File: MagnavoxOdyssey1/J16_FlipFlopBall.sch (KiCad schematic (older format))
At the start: 15 parts

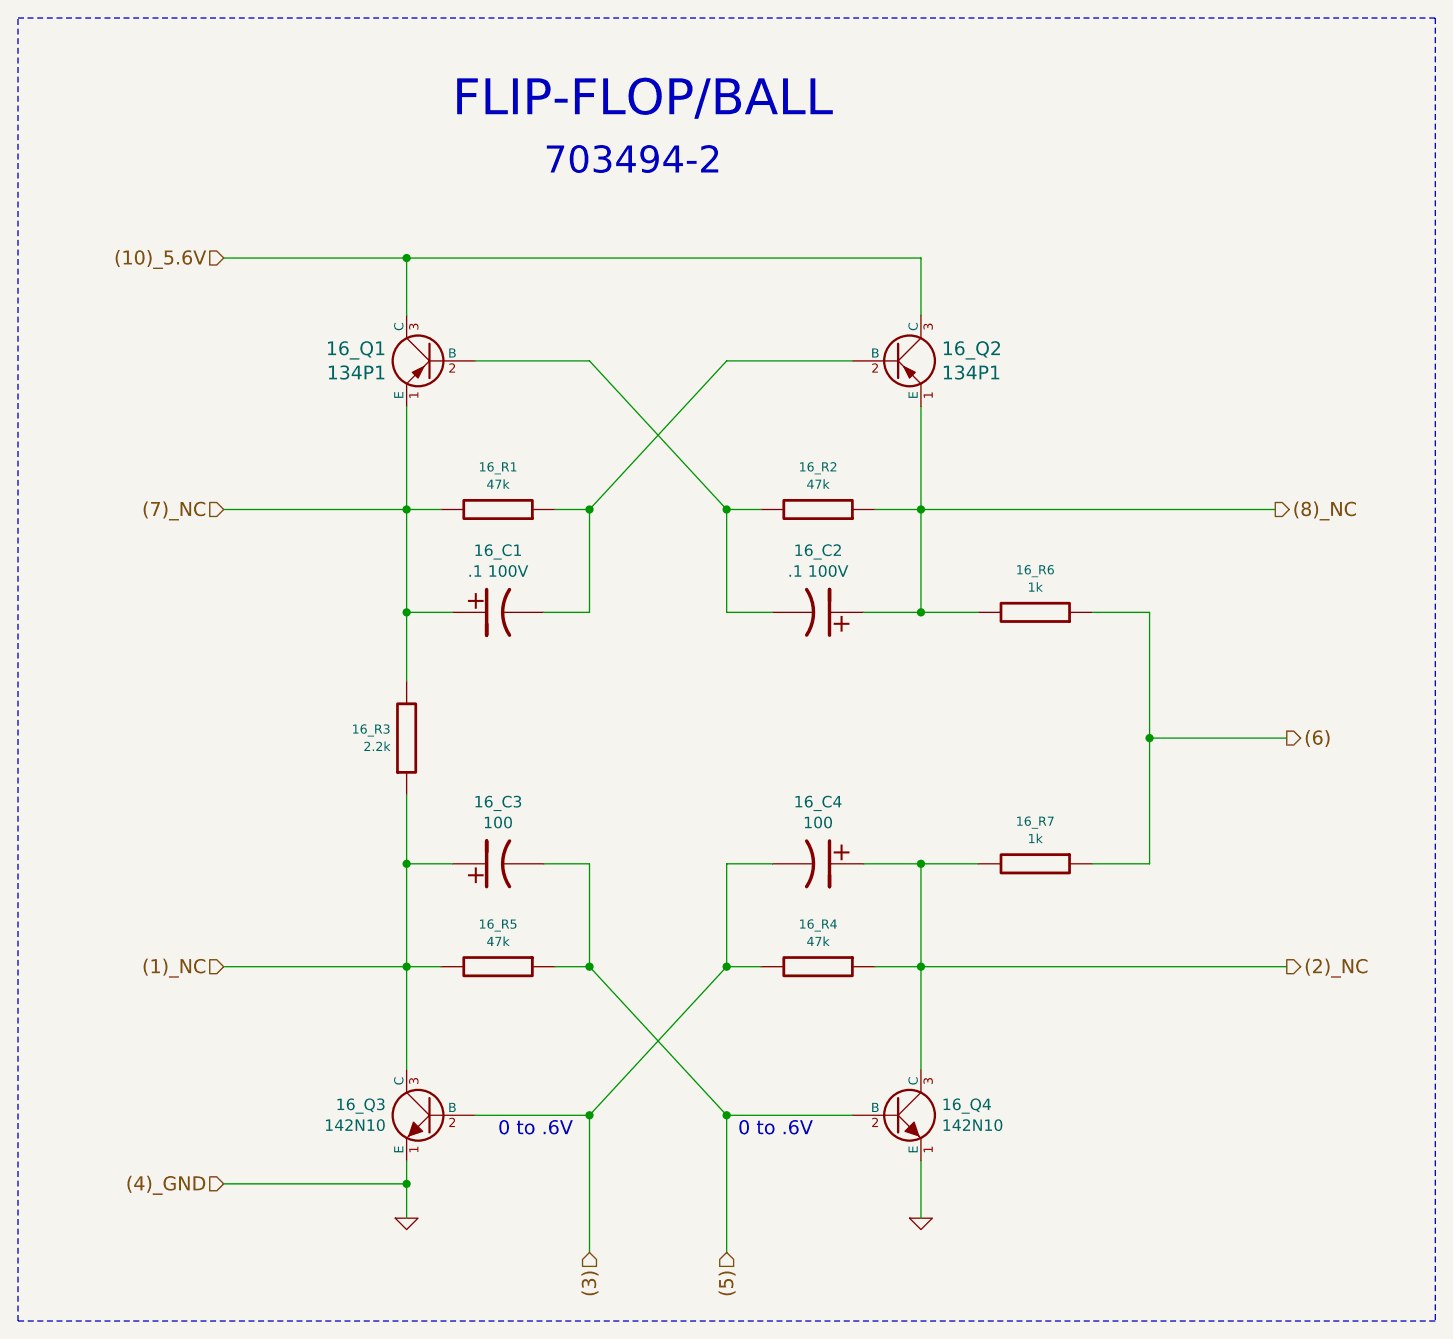
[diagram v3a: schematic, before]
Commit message: terminei de transcrever a PCB toda. Deixei de fora de propósito o estágio de modulação RF do sinal. É pouca coisa, posso adicionar amanhã ou depois... Gerei também um PDFão
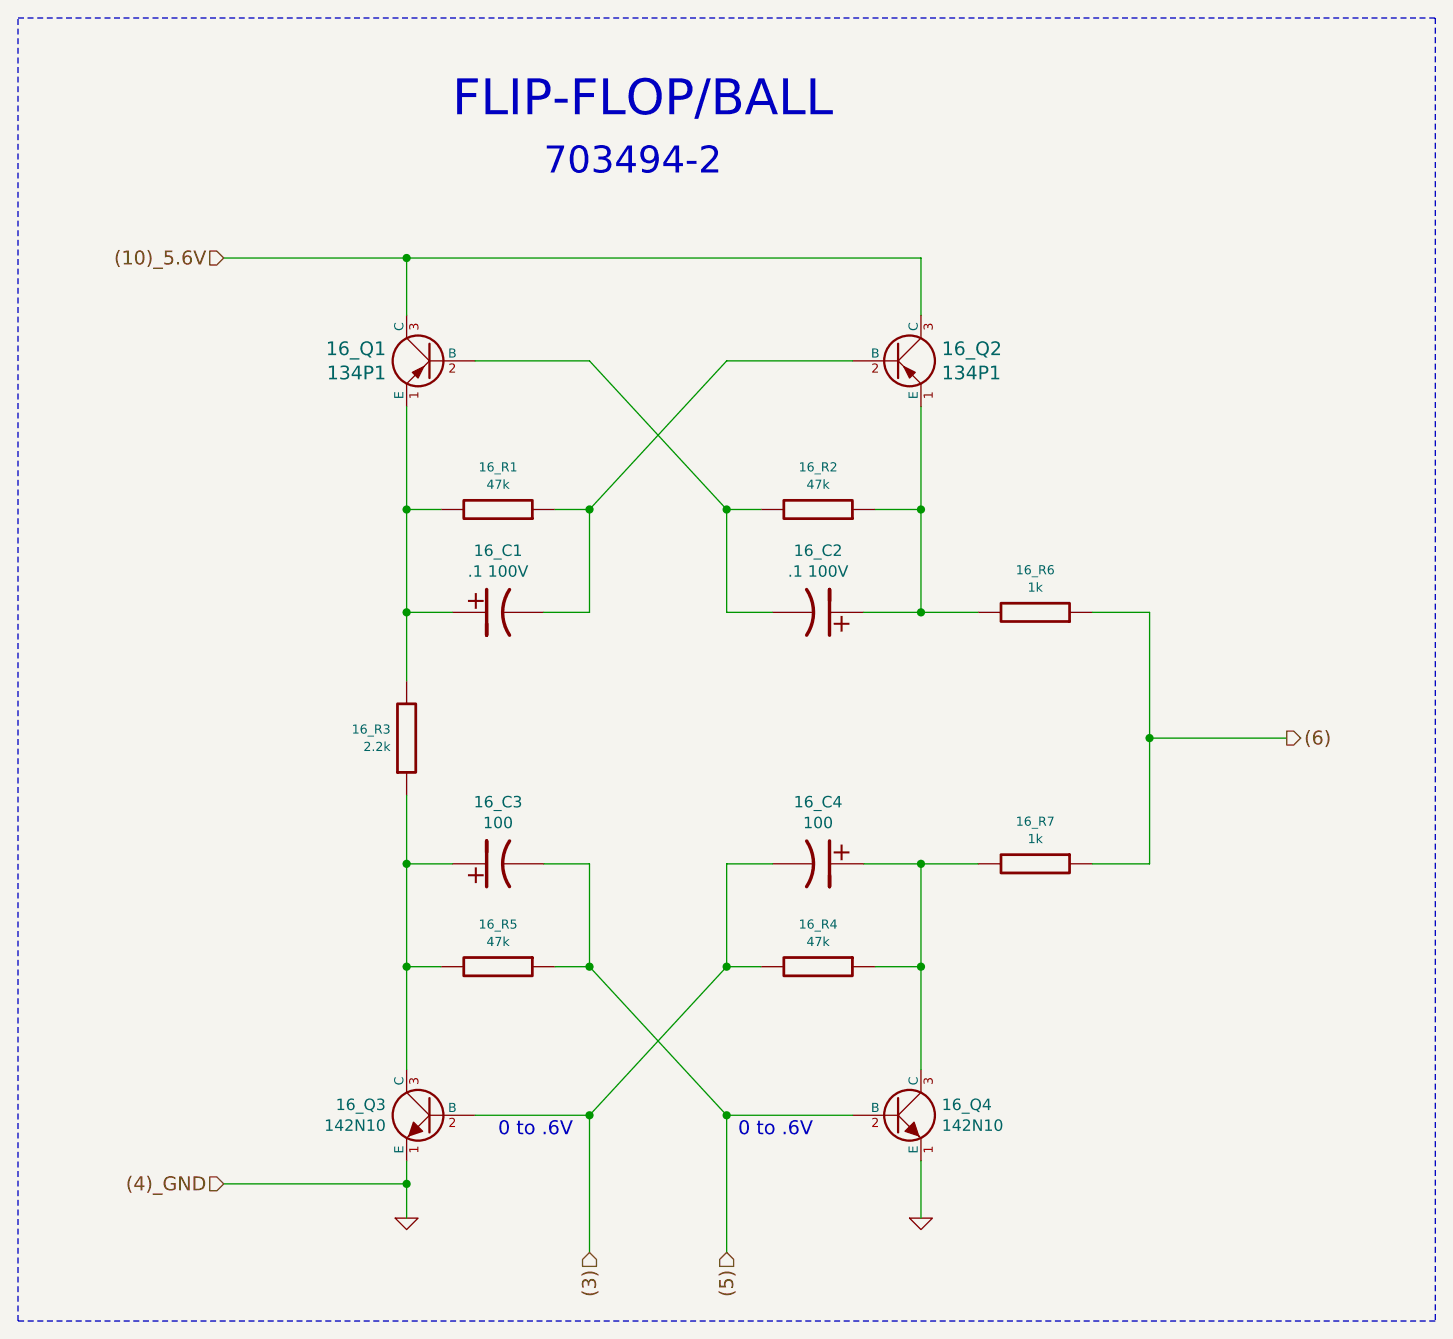
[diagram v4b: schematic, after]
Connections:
- net (1)_NC: no longer names the net of 16_C3.1, 16_Q3.3 (C), 16_R3.1, 16_R5.2
- net (2)_NC: no longer names the net of 16_C4.1, 16_Q4.3 (C), 16_R4.1, 16_R7.2
- net (7)_NC: no longer names the net of 16_C1.1, 16_Q1.1 (E), 16_R1.2, 16_R3.2
- net (8)_NC: no longer names the net of 16_C2.1, 16_Q2.1 (E), 16_R2.1, 16_R6.2
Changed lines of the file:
@@
 $Descr A4 11693 8268
 encoding utf-8
-Sheet 7 10
+Sheet 7 12
 Title ""
 Date ""
@@
 	6450 4350 6450 5250
 Wire Wire Line
-	6250 4800 8050 4800
-Wire Wire Line
-	3400 4800 4350 4800
-Wire Wire Line
 	4200 4050 4200 5250
 Wire Wire Line
@@
 	6450 2350 6450 3250
 Wire Wire Line
-	6250 2800 8000 2800
-Wire Wire Line
-	3400 2800 4350 2800
-Wire Wire Line
 	4200 2350 4200 3550
 Wire Wire Line
@@
 	8050 3800 7450 3800
 Connection ~ 7450 3800
-Text HLabel 8000 2800 2    61   Output ~ 0
-(8)_NC
-Text HLabel 8050 4800 2    61   Output ~ 0
-(2)_NC
 $Comp
 L PNP 16_Q2
@@
 (10)_5.6V
 Connection ~ 4200 1700
-Text HLabel 3400 4800 0    61   Input ~ 0
-(1)_NC
-Text HLabel 3400 2800 0    61   Input ~ 0
-(7)_NC
 Wire Wire Line
 	4400 4350 4200 4350
 $Comp
-L GND #PWR041
+L GND #PWR067
 U 1 1 588FE5F6
 P 4200 5900
-F 0 "#PWR041" H 4200 5900 30  0001 C CNN
+F 0 "#PWR067" H 4200 5900 30  0001 C CNN
 F 1 "GND" H 4200 5830 30  0001 C CNN
 F 2 "" H 4200 5900 60  0001 C CNN
@@
 Connection ~ 4200 5750
 $Comp
-L GND #PWR042
+L GND #PWR068
 U 1 1 588FE81C
 P 6450 5900
-F 0 "#PWR042" H 6450 5900 30  0001 C CNN
+F 0 "#PWR068" H 6450 5900 30  0001 C CNN
 F 1 "GND" H 6450 5830 30  0001 C CNN
 F 2 "" H 6450 5900 60  0001 C CNN
@@
 Text Notes 5650 5550 0    61   ~ 0
 0 to .6V
+Wire Wire Line
+	6450 4800 6250 4800
+Wire Wire Line
+	6450 2800 6250 2800
+Wire Wire Line
+	4200 4800 4350 4800
+Wire Wire Line
+	4200 2800 4350 2800
 $EndSCHEMATC
